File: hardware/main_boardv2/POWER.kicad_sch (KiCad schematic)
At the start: 7 parts, among them J201 USB_C_Receptacle_USB2.0_16P

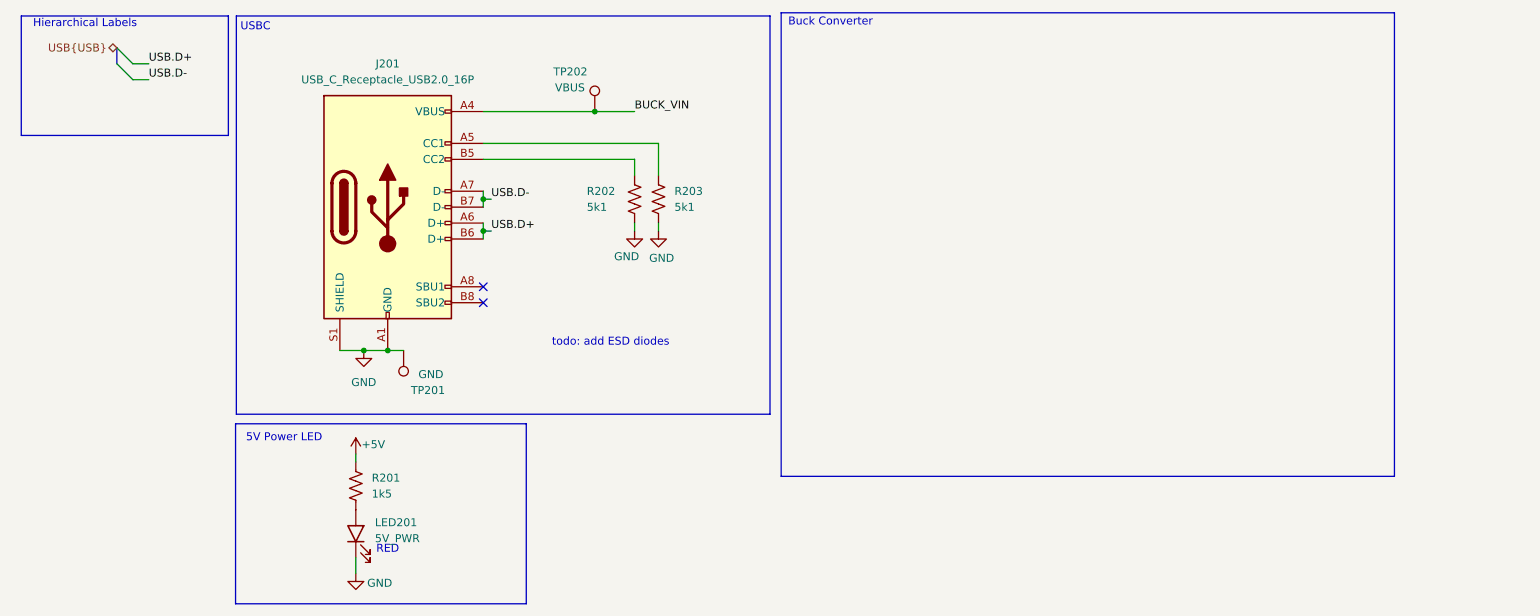
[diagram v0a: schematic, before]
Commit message: dubious hardware schematic 'done'. need to go back and revise passives and verify IC connections, esp the DAC. modified readme
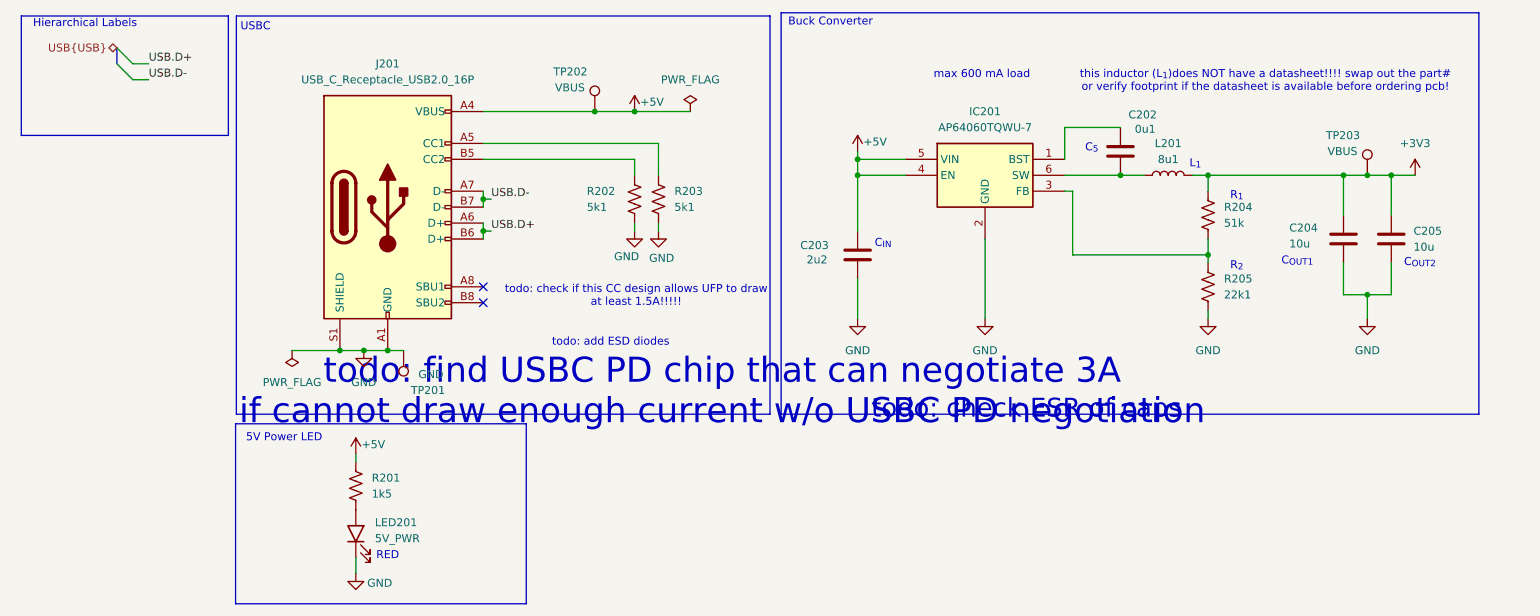
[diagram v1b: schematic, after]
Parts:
- added C202: 0u1, Capacitor_SMD:C_0805_2012Metric, symbol ECE445L:C
- added C203: 2u2, Capacitor_SMD:C_0805_2012Metric, symbol ECE445L:C
- added C204, C205: 10u, Capacitor_SMD:C_0805_2012Metric, symbol ECE445L:C
- added IC201: AP64060TQWU-7, SamacSys_Parts:SOT95P280X100-6N, symbol SamacSys_Parts:AP64060TQWU-7
- added L201: 8u1, Inductor_SMD:L_TDK_SLF12575, symbol Device:L
- added R204: 51k, Resistor_SMD:R_0805_2012Metric, symbol Device:R_US
- added R205: 22k1, Resistor_SMD:R_0805_2012Metric, symbol Device:R_US
- added TP203: VBUS, SamacSys_Parts:bettertestpoint2, symbol Connector:TestPoint
- J201: Mouser Stock/Price https://www.mouser.co.uk/ProductDetail/Same-Sky/UJ20-C-H-G-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 -> https://www.mouser.com/ProductDetail/Same-Sky/UJ20-C-H-G-SM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
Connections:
- net BUCK_VIN is gone; now on net +5V: J201.A4 (VBUS), J201.A9 (VBUS), J201.B4 (VBUS), J201.B9 (VBUS), TP202.1
- net +5V: now also C203.2, IC201.4 (EN), IC201.5 (VIN)
- net GND: now also C203.1, C204.2, C205.2, IC201.2 (GND), R205.2
- new net: C202.1, IC201.6 (SW), L201.1
- new net: C202.2, IC201.1 (BST)
- new net: IC201.3 (FB), R204.2, R205.1
- new net +3V3: C204.1, C205.1, L201.2, R204.1, TP203.1
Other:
- note added: "C_{5}"
- note added: "C_{IN}"
- note added: "C_{OUT1}"
- note added: "C_{OUT2}"
- note added: "L_{1}"
- note added: "R_{1}"
- note added: "R_{2}"
- note added: "max 600 mA load"
- note added: "this inductor (L_{1})does NOT have a datasheet!!!! swap out the part# or verify footprint if the datasheet is available before ordering pcb!"
- note added: "todo: check ESR of caps"
- note added: "todo: check if this CC design allows UFP to draw at least 1.5A!!!!!"
- note added: "todo: find USBC PD chip that can negotiate 3A if cannot draw enough current w/o USBC PD negotiation"

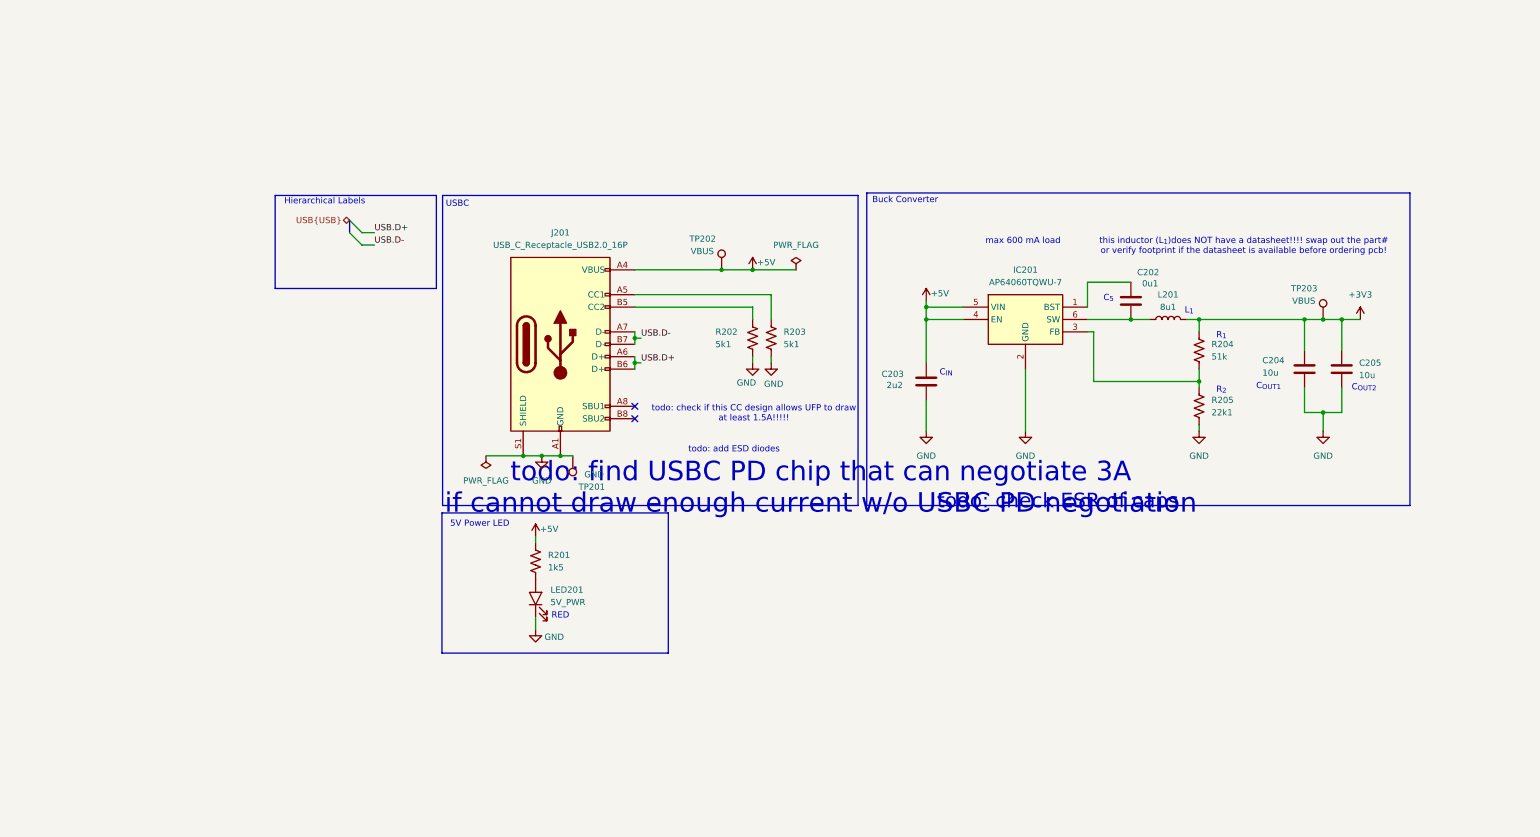
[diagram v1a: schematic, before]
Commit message: schematic sorta done? resized all RC packages to 0805
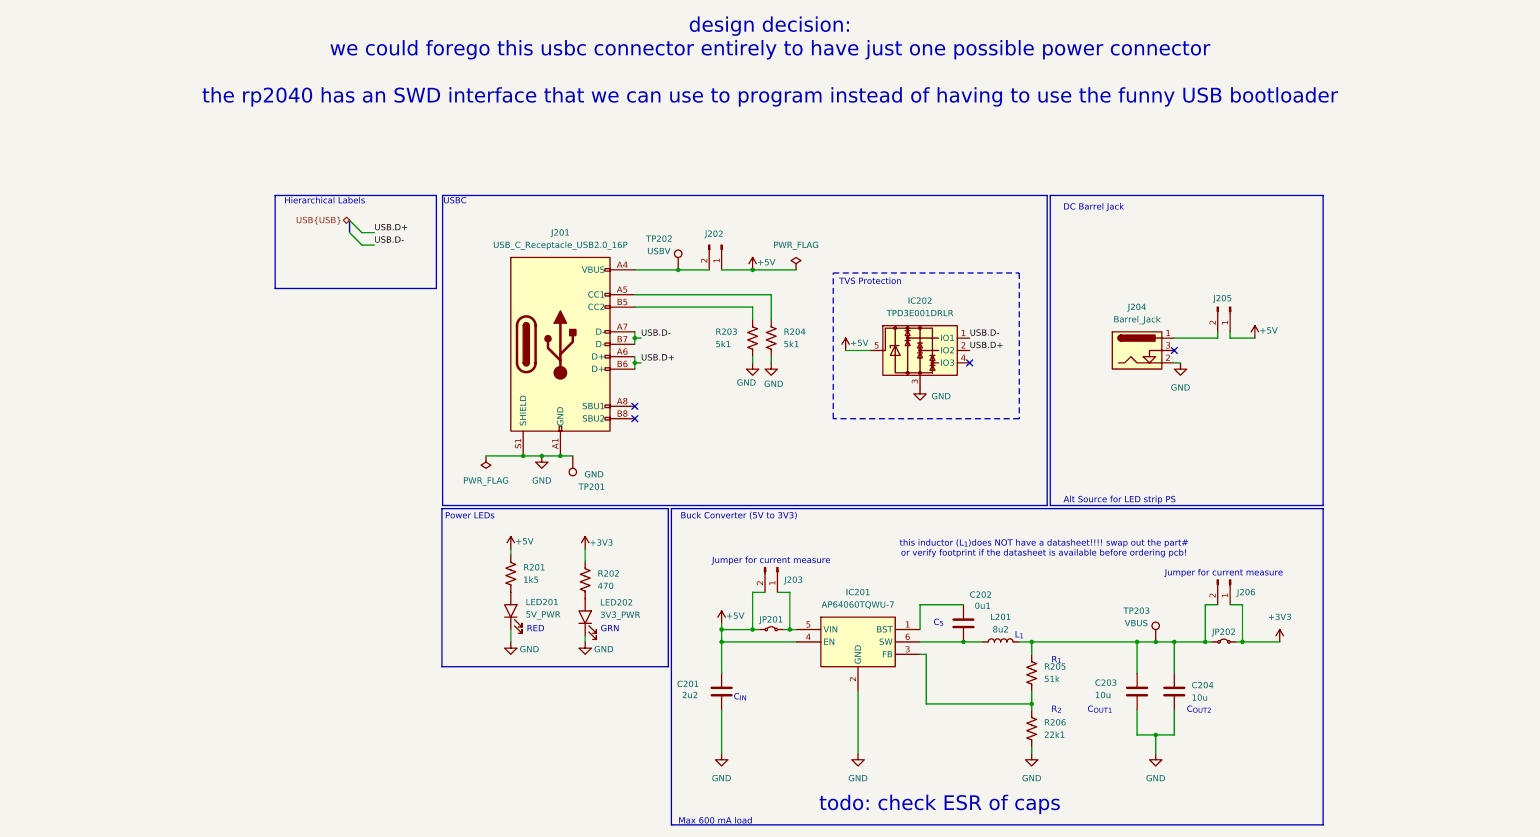
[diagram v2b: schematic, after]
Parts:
- added IC202: TPD3E001DRLR, SOTFL50P160X60-5N, symbol Power_Protection:TPD3E001DRLR
- added J202, J205: SWD Breakout, Connector_PinHeader_2.54mm:PinHeader_1x02_P2.54mm_Vertical, symbol Connector:Conn_01x02_Pin
- added J203, J206: Conn_01x02_Pin, Connector_PinHeader_2.54mm:PinHeader_1x02_P2.54mm_Vertical, symbol Connector:Conn_01x02_Pin
- added J204: Barrel_Jack, SamacSys_Parts:373, symbol SamacSys_Parts:Barrel_Jack
- added JP201, JP202: Jumper_2_Small_Bridged, Jumper:SolderJumper-2_P1.3mm_Bridged2Bar_RoundedPad1.0x1.5mm, symbol Jumper:Jumper_2_Small_Bridged
- added LED202: 3V3_PWR, SamacSys_Parts:LEDC2012X40N, symbol ECE445L:LED
- added R202: 470, Resistor_SMD:R_0805_2012Metric, symbol Device:R_US
- L201: value 8u1 -> 8u2; footprint Inductor_SMD:L_TDK_SLF12575 -> Inductor_SMD:L_Abracon_ASPI-4030S; Mouser Stock/Price https://www.mouser.com/ProductDetail/Eaton-Electronics/HPAL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 -> https://www.mouser.com/ProductDetail/ABRACON/ASPI-4030S-8R2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
- TP202: value VBUS -> USBV
- renumbered C203 to C201, C204 to C203, C205 to C204, R202 to R203, R203 to R204, R204 to R205, R205 to R206
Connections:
- net +3V3: now also J206.1 (Pin_1), JP202.2 (B), R202.1; no longer C203.1, C204.1, L201.2, R205.1, TP203.1
- net +5V: now also IC202.5, J202.1 (Pin_1), J203.2 (Pin_2), J205.1 (Pin_1), JP201.1 (A); no longer IC201.5 (VIN), J201.A4 (VBUS), J201.A9 (VBUS), J201.B4 (VBUS), J201.B9 (VBUS), TP202.1
- net GND: now also IC202.3, J204.2, LED202.1 (K)
- net USB.D+: now also IC202.2 (IO2)
- net USB.D-: now also IC202.1 (IO1)
- new net: LED202.2 (A), R202.2
- new net: IC201.5 (VIN), J203.1 (Pin_1), JP201.2 (B)
- new net: J204.1, J205.2 (Pin_2)
- new net: J201.A4 (VBUS), J201.A9 (VBUS), J201.B4 (VBUS), J201.B9 (VBUS), J202.2 (Pin_2), TP202.1
- new net: C203.1, C204.1, J206.2 (Pin_2), JP202.1 (A), L201.2, R205.1, TP203.1
- no-connect marks 2 -> 4
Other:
- note added: "Alt Source for LED strip PS"
- note added: "Buck Converter (5V to 3V3)"
- note added: "DC Barrel Jack"
- note added: "GRN"
- note added: "Jumper for current measure"
- note added: "Max 600 mA load"
- note added: "Power LEDs"
- note added: "TVS Protection"
- note added: "design decision: we could forego this usbc connector entirely to have just one possible power connector the rp2040 has an SWD interface that we can use to program instead of having to use the funny USB bootloader"
- note removed: "5V Power LED"
- note removed: "Buck Converter"
- note removed: "max 600 mA load"
- note removed: "todo: add ESD diodes"
- note removed: "todo: check if this CC design allows UFP to draw at least 1.5A!!!!!"
- note removed: "todo: find USBC PD chip that can negotiate 3A if cannot draw enough current w/o USBC PD negotiation"
- moved on the sheet: C201, C202, C203, C204, IC201, L201, LED201, R201, R205, R206, TP202, TP203

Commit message: resized all package to 0603
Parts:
- C201: footprint Capacitor_SMD:C_0805_2012Metric -> Capacitor_SMD:C_0603_1608Metric; Mouser Price/Stock 2 -> (none)
- C202: footprint Capacitor_SMD:C_0805_2012Metric -> Capacitor_SMD:C_0603_1608Metric; Mouser Price/Stock https://www.mouser.com/ProductDetail/Walsin/MG21B104K500CT?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 -> (none)
- C203, C204: footprint Capacitor_SMD:C_0805_2012Metric -> Capacitor_SMD:C_0603_1608Metric; Mouser Price/Stock https://www.mouser.com/ProductDetail/Samsung-Electro-Mechan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 -> (none)
- R201: footprint Resistor_SMD:R_0805_2012Metric -> Resistor_SMD:R_0603_1608Metric; Mouser Price/Stock https://www.mouser.com/ProductDetail/ROHM-Semiconductor/ESR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 -> (none)
- R202, R203, R204: footprint Resistor_SMD:R_0805_2012Metric -> Resistor_SMD:R_0603_1608Metric; Mouser Price/Stock https://www.mouser.com/ProductDetail/YAGEO/AF0805JR-07470RL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 -> (none)
- R205, R206: footprint Resistor_SMD:R_0805_2012Metric -> Resistor_SMD:R_0603_1608Metric
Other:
- note added: "1 - V+ 2 - GND 3 - Breaks contact when plug insert"
- note added: "TODO: verify this"
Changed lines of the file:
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@@
 	(text "USBC"
 		(exclude_from_sim no)
-		(at 50.8 15.24 0)
+		(at 51.562 15.494 0)
 		(effects
 			(font
@@
 		)
 	)
+	(text "TODO: verify this"
+		(exclude_from_sim no)
+		(at 217.424 29.972 0)
+		(effects
+			(font
+				(size 3 3)
+			)
+		)
+	)
 	(text "GRN"
 		(exclude_from_sim no)
@@
 		)
 	)
+	(text "1 - V+\n2 - GND\n3 - Breaks contact when plug insert"
+		(exclude_from_sim no)
+		(at 173.736 70.612 0)
+		(effects
+			(font
+				(size 1.27 1.27)
+			)
+			(justify left)
+		)
+	)
 	(text "design decision:\nwe could forego this usbc connector entirely to have just one possible power connector\n\nthe rp2040 has an SWD interface that we can use to program instead of having to use the funny USB bootloader"
 		(exclude_from_sim no)
@@
 			)
 		)
-		(property "Footprint" "Resistor_SMD:R_0805_2012Metric"
+		(property "Footprint" "Resistor_SMD:R_0603_1608Metric"
 			(at 116.586 43.434 90)
 			(effects
@@
 			)
 		)
-		(property "Mouser Price/Stock" "https://www.mouser.com/ProductDetail/YAGEO/AF0805JR-07470RL?qs=tggtontpCXOaQg0VhtuXeg%3D%3D"
+		(property "Mouser Price/Stock" ""
 			(at 115.57 43.18 0)
 			(effects
@@
 			)
 		)
-		(property "Footprint" "Resistor_SMD:R_0805_2012Metric"
+		(property "Footprint" "Resistor_SMD:R_0603_1608Metric"
 			(at 78.486 92.964 90)
 			(effects
@@
 			)
 		)
-		(property "Mouser Price/Stock" "https://www.mouser.com/ProductDetail/YAGEO/AF0805JR-07470RL?qs=tggtontpCXOaQg0VhtuXeg%3D%3D"
+		(property "Mouser Price/Stock" ""
 			(at 77.47 92.71 0)
 			(effects
@@
 			)
 		)
-		(property "Footprint" "Resistor_SMD:R_0805_2012Metric"
+		(property "Footprint" "Resistor_SMD:R_0603_1608Metric"
 			(at 63.246 91.694 90)
 			(effects
@@
 			)
 		)
-		(property "Mouser Price/Stock" "https://www.mouser.com/ProductDetail/ROHM-Semiconductor/ESR03EZPJ152?qs=DyUWGjl%252BcVvm2NOHIcQYzQ%3D%3D"
+		(property "Mouser Price/Stock" ""
 			(at 62.23 91.44 0)
 			(effects
@@
 			)
 		)
-		(property "Footprint" "Capacitor_SMD:C_0805_2012Metric"
+		(property "Footprint" "Capacitor_SMD:C_0603_1608Metric"
 			(at 153.9748 97.79 0)
 			(effects
@@
 			)
 		)
-		(property "Mouser Price/Stock" "https://www.mouser.com/ProductDetail/Walsin/MG21B104K500CT?qs=sGAEpiMZZMt7gvpyg0xT8jBHDtGZvLzXjlSfFWC8Jgc2tQbZi0zprA%3D%3D"
+		(property "Mouser Price/Stock" ""
 			(at 154.94 101.6 90)
 			(effects
@@
 			)
 		)
-		(property "Footprint" "Capacitor_SMD:C_0805_2012Metric"
+		(property "Footprint" "Capacitor_SMD:C_0603_1608Metric"
 			(at 104.4448 111.76 0)
 			(effects
@@
 			)
 		)
-		(property "Mouser Price/Stock" "2"
+		(property "Mouser Price/Stock" ""
 			(at 105.41 115.57 90)
 			(effects
@@
 			)
 		)
-		(property "Footprint" "Capacitor_SMD:C_0805_2012Metric"
+		(property "Footprint" "Capacitor_SMD:C_0603_1608Metric"
 			(at 199.0852 119.38 0)
 			(effects
@@
 			)
 		)
-		(property "Mouser Price/Stock" "https://www.mouser.com/ProductDetail/Samsung-Electro-Mechanics/CL21A106KPFNNNE?qs=sGAEpiMZZMt7gvpyg0xT8jBAVP%252BdkPhuUJvUBe19zr8%3D"
+		(property "Mouser Price/Stock" ""
 			(at 198.12 115.57 0)
 			(effects
@@
 			)
 		)
-		(property "Footprint" "Capacitor_SMD:C_0805_2012Metric"
+		(property "Footprint" "Capacitor_SMD:C_0603_1608Metric"
 			(at 191.4652 119.38 0)
 			(effects
@@
 			)
 		)
-		(property "Mouser Price/Stock" "https://www.mouser.com/ProductDetail/Samsung-Electro-Mechanics/CL21A106KPFNNNE?qs=sGAEpiMZZMt7gvpyg0xT8jBAVP%252BdkPhuUJvUBe19zr8%3D"
+		(property "Mouser Price/Stock" ""
 			(at 190.5 115.57 0)
 			(effects
@@
 			)
 		)
-		(property "Footprint" "Resistor_SMD:R_0805_2012Metric"
+		(property "Footprint" "Resistor_SMD:R_0603_1608Metric"
 			(at 112.776 43.434 90)
 			(effects
@@
 			)
 		)
-		(property "Mouser Price/Stock" "https://www.mouser.com/ProductDetail/YAGEO/AF0805JR-07470RL?qs=tggtontpCXOaQg0VhtuXeg%3D%3D"
+		(property "Mouser Price/Stock" ""
 			(at 111.76 43.18 0)
 			(effects
@@
 			)
 		)
-		(property "Footprint" "Resistor_SMD:R_0805_2012Metric"
+		(property "Footprint" "Resistor_SMD:R_0603_1608Metric"
 			(at 169.926 112.014 90)
 			(effects
@@
 			)
 		)
-		(property "Footprint" "Resistor_SMD:R_0805_2012Metric"
+		(property "Footprint" "Resistor_SMD:R_0603_1608Metric"
 			(at 169.926 123.444 90)
 			(effects
